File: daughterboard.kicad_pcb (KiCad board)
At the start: 6 copper layers, 49 x 49 mm, 58 parts, among them J1 USB_C_Receptacle_USB2.0, J10 Conn_01x14, J3 Conn_01x38, J4 Conn_01x22, J5 Conn_02x11, J6 Conn_01x38, J7 Conn_01x38, J8 Conn_01x38, J9 Conn_01x14, Q1 PMOS, Q2 PMOS, Q3 NMOS, U1 LFE5U-12F-6BG256C, U2 AT25SF081-SSHD-X, U3 AMS1117-3.3, U4 TPS74611PQWDRBRQ1, U5 XC6206P252MR

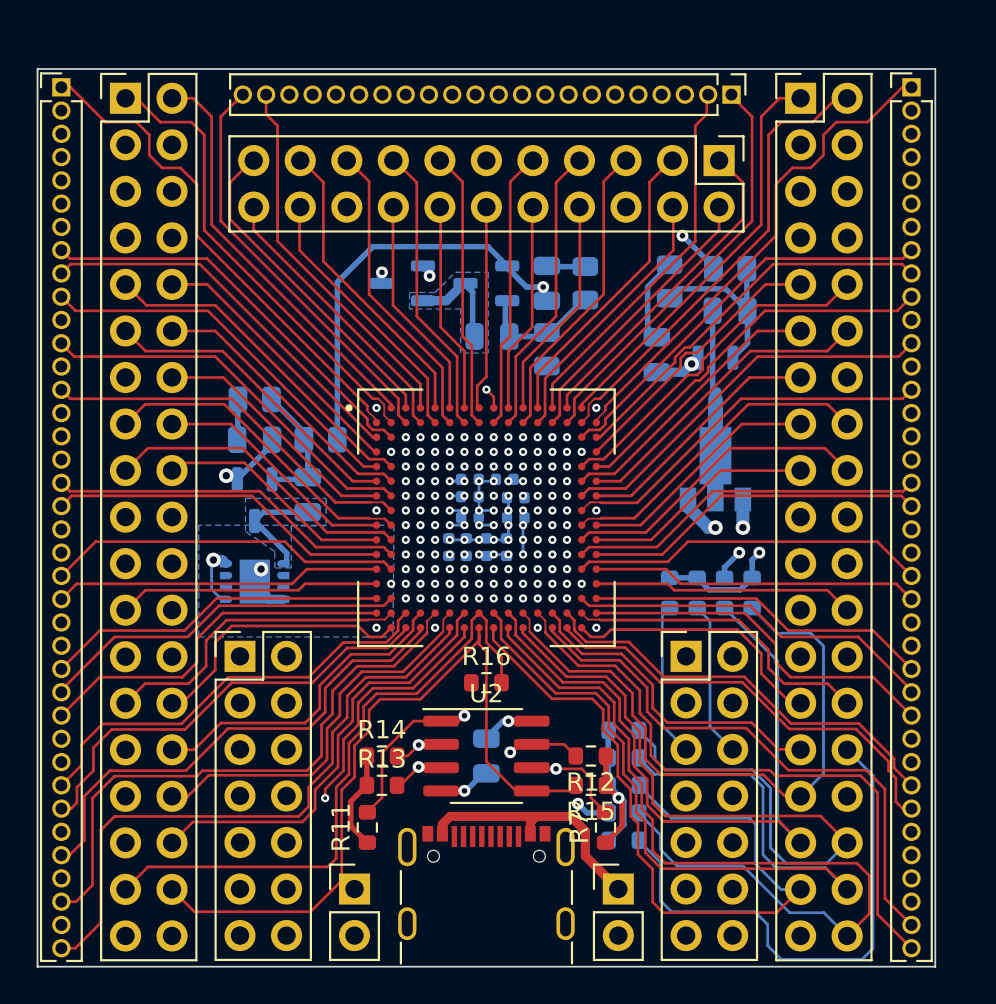
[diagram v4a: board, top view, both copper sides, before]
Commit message: Route power, FTDI chip
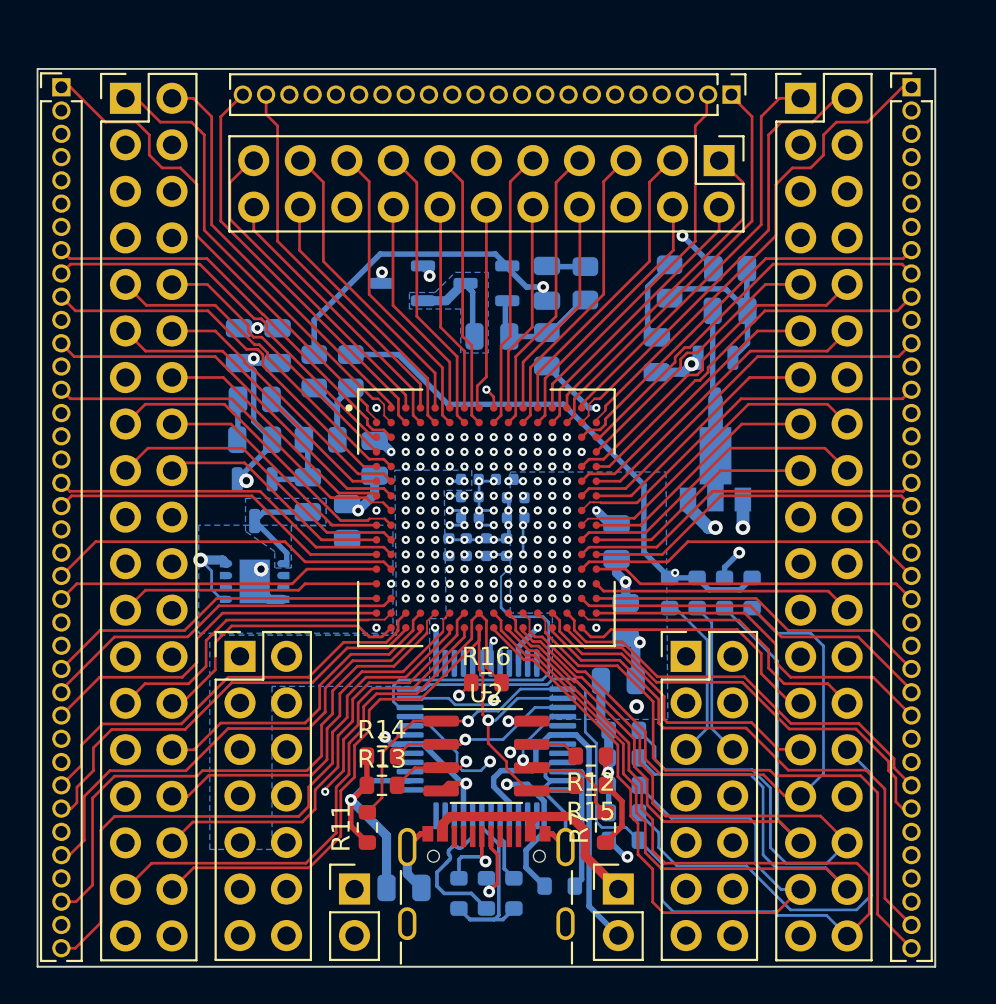
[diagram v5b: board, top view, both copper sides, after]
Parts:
- added C1: 10uF, Capacitor_SMD:C_0805_2012Metric, B.Cu at (92.4, 100.2)
- added C19: 10uF, Capacitor_SMD:C_0805_2012Metric, B.Cu at (86.5, 90.6)
- added C20: 10uF, Capacitor_SMD:C_0805_2012Metric, B.Cu at (107.6, 105.6)
- added C21: 10uF, Capacitor_SMD:C_0805_2012Metric, B.Cu at (95.5, 120.2)
- added C22: 10uF, Capacitor_SMD:C_0805_2012Metric, B.Cu at (107.1, 101.3)
- added C23: 10uF, Capacitor_SMD:C_0805_2012Metric, B.Cu at (88.6, 90.6)
- added C24: 10uF, Capacitor_SMD:C_0805_2012Metric, B.Cu at (93.9, 96.8)
- added R23: ~, Resistor_SMD:R_0805_2012Metric, B.Cu at (90.6, 92.0)
- added R24: ~, Resistor_SMD:R_0805_2012Metric, B.Cu at (92.6, 92.0)
- added R25: 470, Resistor_SMD:R_0603_1608Metric, B.Cu at (104.0, 120.1)
- added R26: 1.5K, Resistor_SMD:R_0603_1608Metric, B.Cu at (101.5, 120.5)
- added R27: 27, Resistor_SMD:R_0603_1608Metric, B.Cu at (98.5, 120.5)
- added R28: 27, Resistor_SMD:R_0603_1608Metric, B.Cu at (100.0, 120.5)
- added U6: FT2232D, Package_QFP:LQFP-48_7x7mm_P0.5mm, B.Cu at (100.0, 112.1)
- J11, J2: renamed from REF**; value PinHeader_1x02_P2.54mm_Vertical -> Conn_01x02_Pin
- moved C9 8.29 mm to (107.2, 108.9), turned to 0 degrees
- moved R2 1.50 mm to (107.5, 116.1)
- moved R4 1.50 mm to (107.5, 117.6)
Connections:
- net IO0 renamed F_MISO
- net IO1 renamed F_MOSI
- net PROG_CLK renamed F_SCK
- net PROG_FLASH_CS renamed F_CS
- C11 pad 1: +3V0 -> VCCIOA
- C12 pad 1: +2V8 -> VCCIOB
- J1 pad A6: unconnected-(J1-D+-PadA6) -> /JTAG/D+
- J1 pad A7: unconnected-(J1-D--PadA7) -> /JTAG/D-
- J11 pad 1: (no net) -> 5VUSB
- J11 pad 2: (no net) -> 5VREGIN
- J2 pad 1: (no net) -> 3V3REGOUT
- J2 pad 2: (no net) -> 3V3REGIN
- J9 pad 10: VCCIOB -> +3V3
- J9 pad 11: +2V5 -> VCCIOA
- J9 pad 12: +1V1 -> 3V3REGOUT
- J9 pad 7: 3V3REGOUT -> +2V5
- J9 pad 8: +3V3 -> +1V1
- J9 pad 9: VCCIOA -> VCCIOB
- R21 pad 1: +2V5 -> Net-(R21-Pad1)
- U1 pad F10: +3V0 -> VCCIOA
- U1 pad F11: +3V0 -> VCCIOA
- U1 pad F6: +2V8 -> VCCIOB
- U1 pad F7: +2V8 -> VCCIOB
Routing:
- net +3V3: track 34.1 -> 98.9 mm, vias 12 -> 17
- net 3V3REGOUT: track 2.58 -> 49.6 mm
- net +2V5: track 22.8 -> 62.9 mm
- net GND: track 28.2 -> 62.3 mm, vias 34 -> 37
- net VCCIOA: track 0.00 -> 29.2 mm, vias 0 -> 3
- net TMS: track 42.5 -> 70.0 mm, vias 0 -> 1
- net TDI: track 34.9 -> 57.8 mm, vias 0 -> 1
- net +1V1: track 6.90 -> 28.3 mm, vias 7 -> 9
- net 5VREGIN: track 2.37 -> 23.4 mm
- net TCK: track 47.6 -> 66.8 mm
- net TDO: track 55.1 -> 67.4 mm
- net /JTAG/USBD+: track 0.00 -> 11.0 mm
- net F_MOSI: track 36.9 -> 46.2 mm
- net /JTAG/USBD-: track 0.00 -> 8.26 mm
- net Net-(U6-AVCC): track 0.00 -> 7.41 mm
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- added copper zone on In4.Cu, net +1V1
- added copper zone on In1.Cu, net +2V5
- added copper zone on In4.Cu, net +2V5
- added copper zone on In2.Cu, net +3V3
- added copper zone on In4.Cu, net +3V3
- added copper zone on B.Cu, net VCCIOA
- added copper zone on B.Cu, net VCCIOB

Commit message: Silkscreen, more power
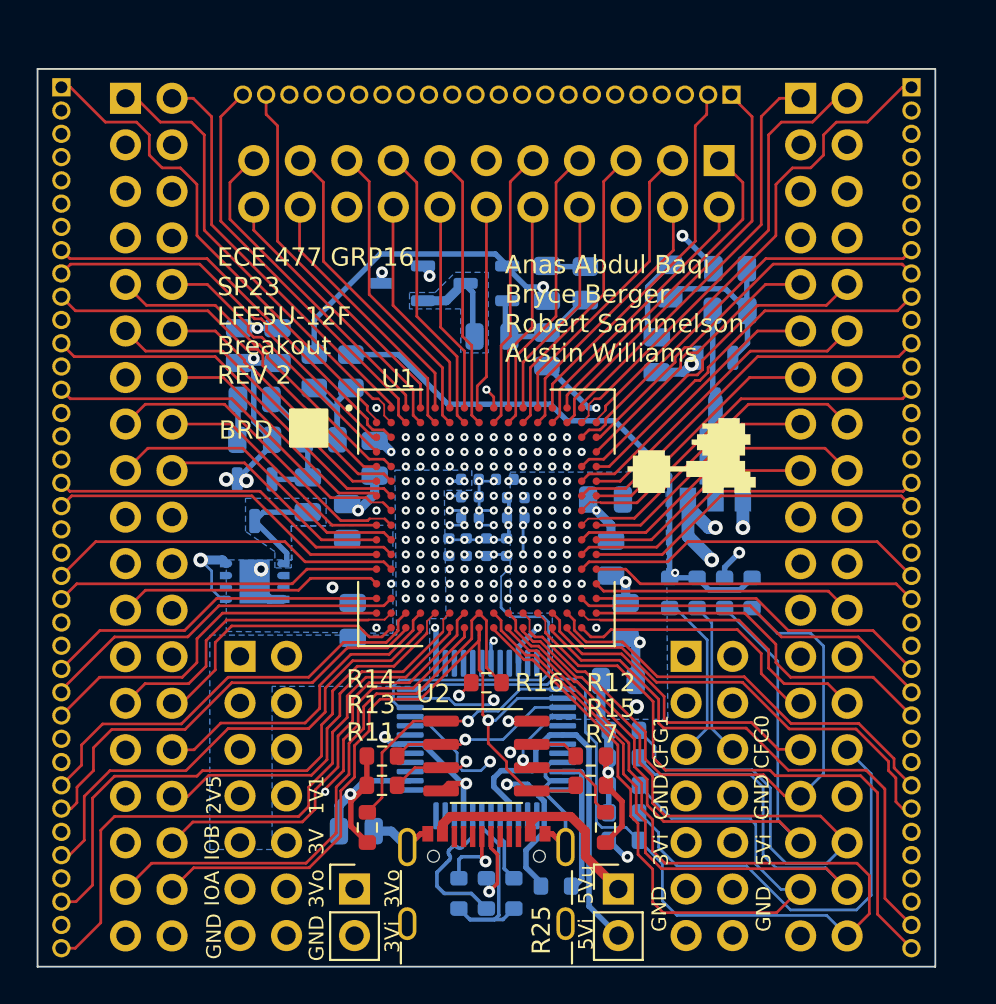
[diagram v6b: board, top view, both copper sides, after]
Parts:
- added C25: 10uF, Capacitor_SMD:C_0805_2012Metric, B.Cu at (106.5, 99.0)
- added C26: 10uF, Capacitor_SMD:C_0805_2012Metric, B.Cu at (92.7, 105.6)
- added G***: LOGO, LOGO, F.Cu at (111.2, 96.6)
- moved C21 4.05 mm to (92.9, 117.1)
- moved C22 0.95 mm to (106.8, 102.2)
- moved R25 0.20 mm to (103.8, 120.1)
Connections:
- U4 pad 1: 1V1REGOUT -> (no net)
- U4 pad 4: GND -> (no net)
- U4 pad 5: 3V3REGIN -> (no net)
- U4 pad 6: unconnected-(U4-PG-Pad6) -> (no net)
- U4 pad 8: 3V3REGIN -> (no net)
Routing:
- net 5VREGIN: track 23.4 -> 27.3 mm, vias 1 -> 2
- net +3V3: track 98.9 -> 95.1 mm
- net GND: track 62.3 -> 63.3 mm, vias 37 -> 38
- net H12: track 34.4 -> 33.4 mm
- net J12: track 34.6 -> 33.8 mm
- net N3: track 19.9 -> 20.7 mm
- net M13: track 14.0 -> 14.7 mm
- net +1V1: track 28.3 -> 28.9 mm, vias 9 -> 10
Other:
- board text added: "1V1"
- board text added: "2V5"
- board text added: "3V"
- board text added: "3Vi"
- board text added: "3Vo"
- board text added: "5Vi"
- board text added: "5Vu"
- board text added: "Anas Abdul Baqi Bryce Berger Robert Sammelson Austin Williams"
- board text added: "BRD"
- board text added: "CFG0"
- board text added: "CFG1"
- board text added: "ECE 477 GRP16 SP23 LFE5U-12F Breakout REV 2"
- board text added: "GND"
- board text added: "IOA"
- board text added: "IOB"
- board text added: "JLCJLCJLCJLC"
